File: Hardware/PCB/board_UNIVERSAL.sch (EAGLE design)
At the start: 10 parts, among them U1 L7805CV

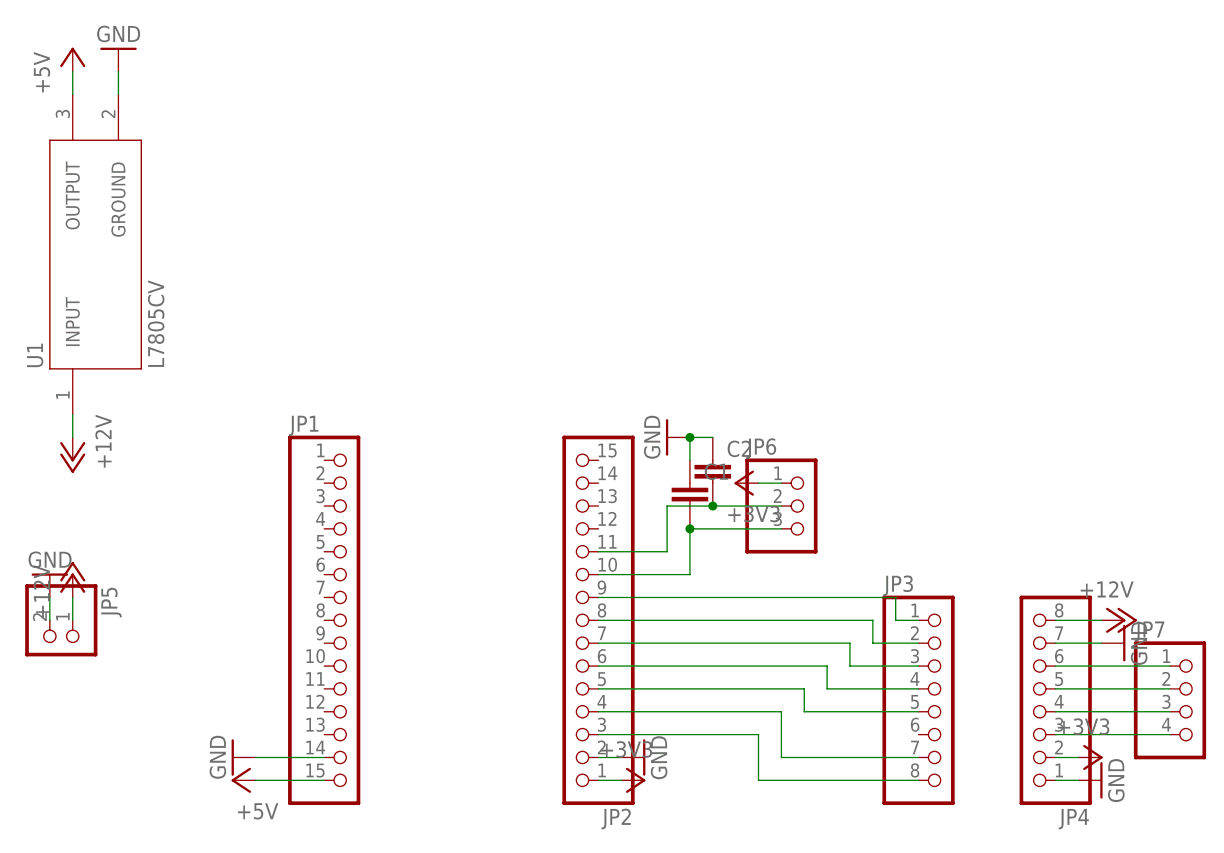
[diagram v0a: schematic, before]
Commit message: Fix by @kswiorek
Created a universal board that connects all the possible setup pins to the ESP (there is a lot GPIO left) and moved the buttons to the other side.
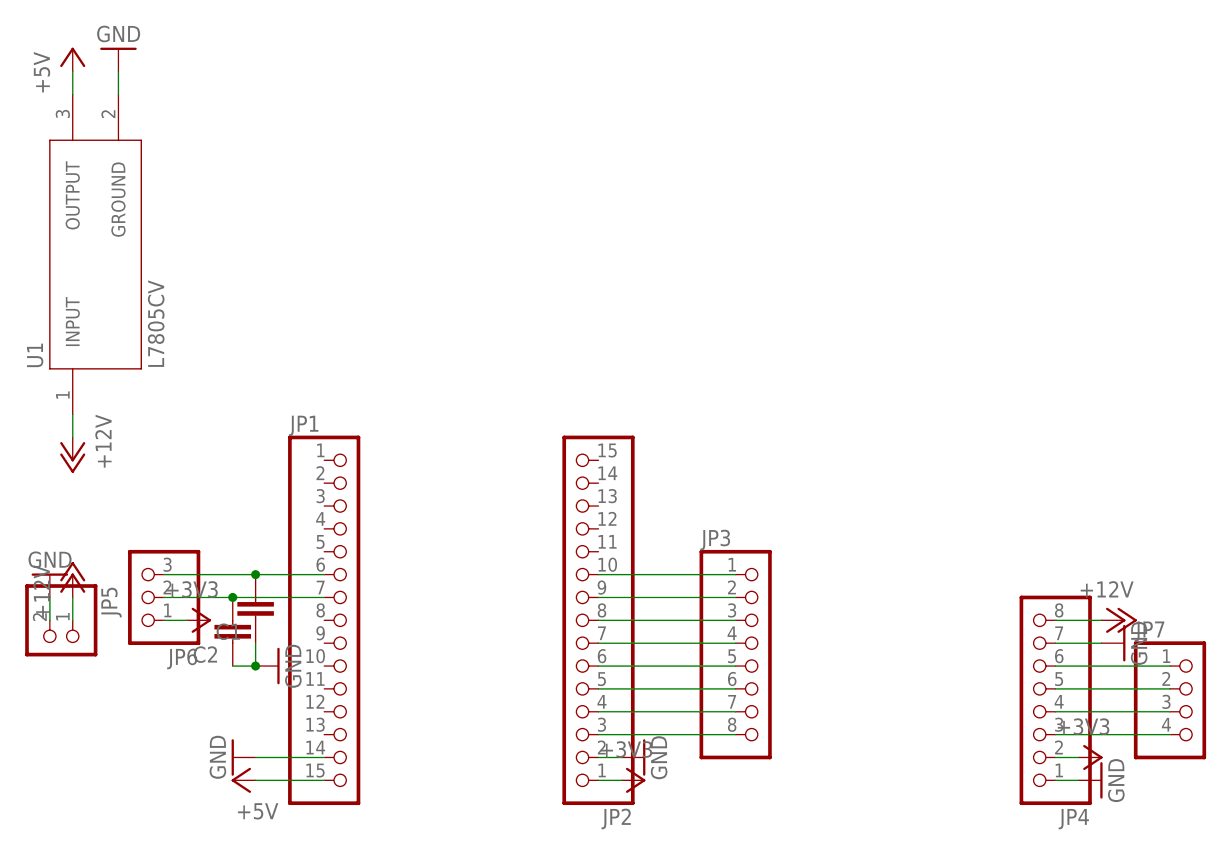
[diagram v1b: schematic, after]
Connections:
- new net N$12: JP2.5, JP3.6
- net N$1: now also JP1.7; no longer JP2.11
- net N$2: now also JP1.6; no longer JP2.10
- net N$3: now also JP2.10; no longer JP2.9
- net N$4: now also JP2.8; no longer JP2.7
- net N$5: now also JP2.7; no longer JP2.6
- net N$6: now also JP2.6; no longer JP2.5
- net N$7: now also JP2.9; no longer JP2.8
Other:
- moved on the sheet: C1, C2, JP3, JP6
